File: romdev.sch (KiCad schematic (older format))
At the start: 38 parts, among them J1 AVR-ISP, J2 USB_B_Micro, J7 SYSRST, U1 ATmega328P-AU, U10 conn2k, U11 conn32k, U2 mcp2221, U3 74HCT157, U4 74HCT595, U5 74HCT595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

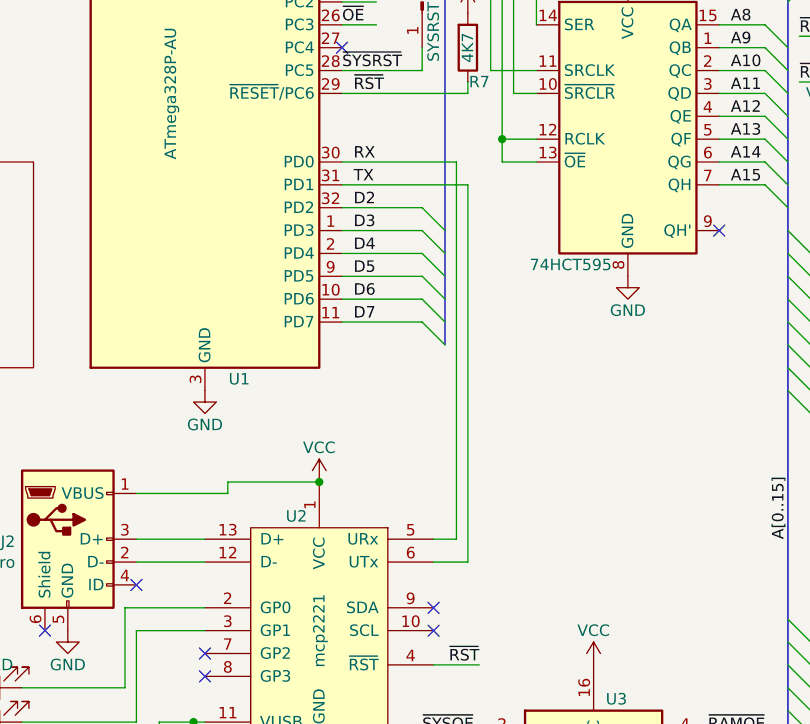
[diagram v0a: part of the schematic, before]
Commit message: fixed swapped RX/TX lines
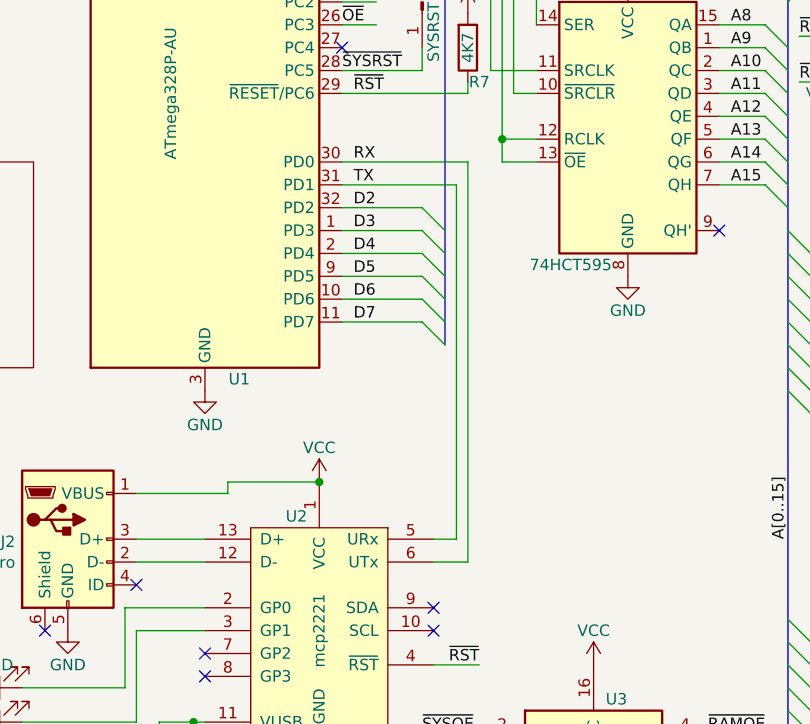
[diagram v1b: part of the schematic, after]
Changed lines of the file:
@@
 NoConn ~ 4450 3750
 Wire Wire Line
-	2800 3450 3300 3450
-Wire Wire Line
-	3300 3450 3300 5100
+	3300 3550 3300 5100
 Text Label 2850 3450 0    50   ~ 0
 RX
@@
 	3300 5100 3200 5100
 Wire Wire Line
-	3350 3550 3350 5200
-Wire Wire Line
 	3350 5200 3200 5200
-Wire Wire Line
-	2800 3550 3350 3550
 Text Label 2850 3550 0    50   ~ 0
 TX
@@
 Wire Wire Line
 	2800 3150 3350 3150
+$Comp
+L power:VCC #PWR032
+U 1 1 60FE6889
+P 3350 2800
+F 0 "#PWR032" H 3350 2650 50  0001 C CNN
+F 1 "VCC" H 3350 2950 50  0000 C CNN
+F 2 "" H 3350 2800 50  0001 C CNN
+F 3 "" H 3350 2800 50  0001 C CNN
+	1    3350 2800
+	1    0    0    -1
+$EndComp
+Wire Wire Line
+	3300 3550 2800 3550
+Wire Wire Line
+	3350 3450 2800 3450
+Wire Wire Line
+	3350 3450 3350 5200
 Wire Bus Line
 	8100 1500 8100 2650
@@
 Wire Bus Line
 	4750 1250 4750 6150
-$Comp
-L power:VCC #PWR032
-U 1 1 60FE6889
-P 3350 2800
-F 0 "#PWR032" H 3350 2650 50  0001 C CNN
-F 1 "VCC" H 3350 2950 50  0000 C CNN
-F 2 "" H 3350 2800 50  0001 C CNN
-F 3 "" H 3350 2800 50  0001 C CNN
-	1    3350 2800
-	1    0    0    -1
-$EndComp
 $EndSCHEMATC

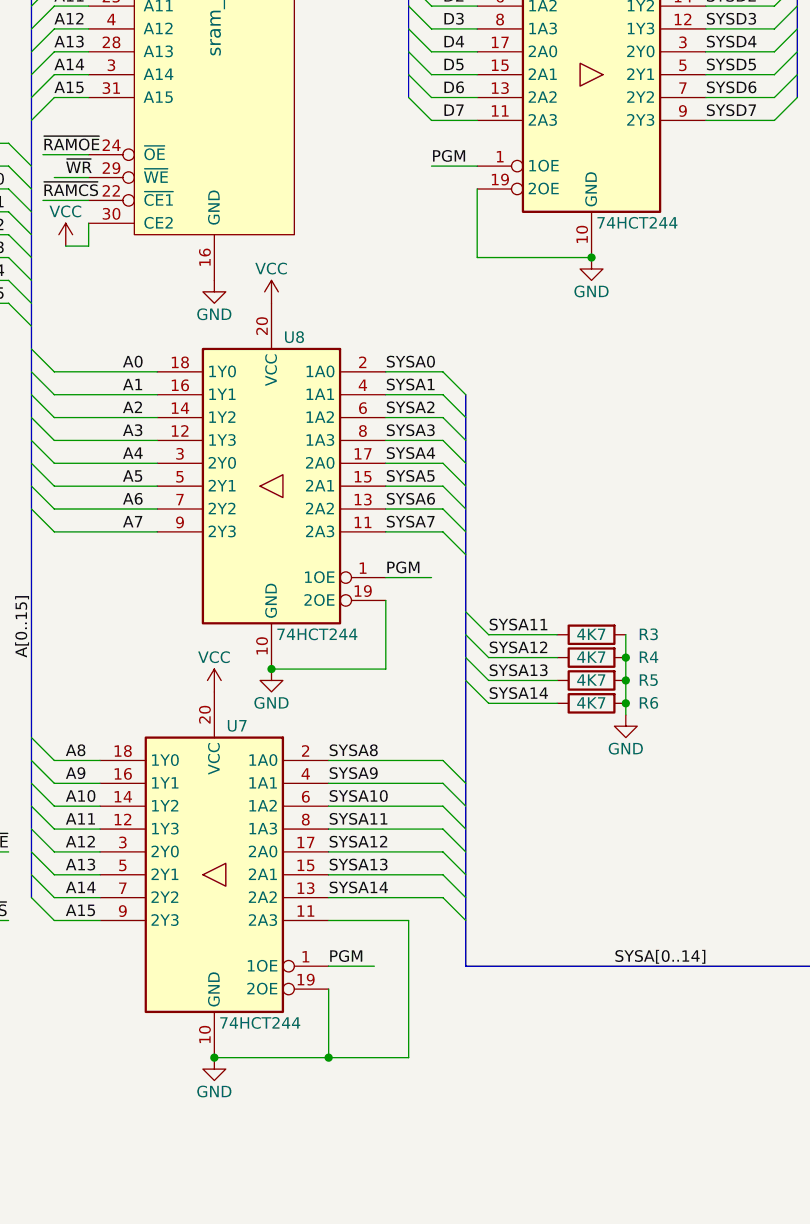
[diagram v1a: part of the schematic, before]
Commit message: - fixed mistake tying half the tri-state buffer bits to always on - fixed firmware bugs, now it can program and readback memory correctly
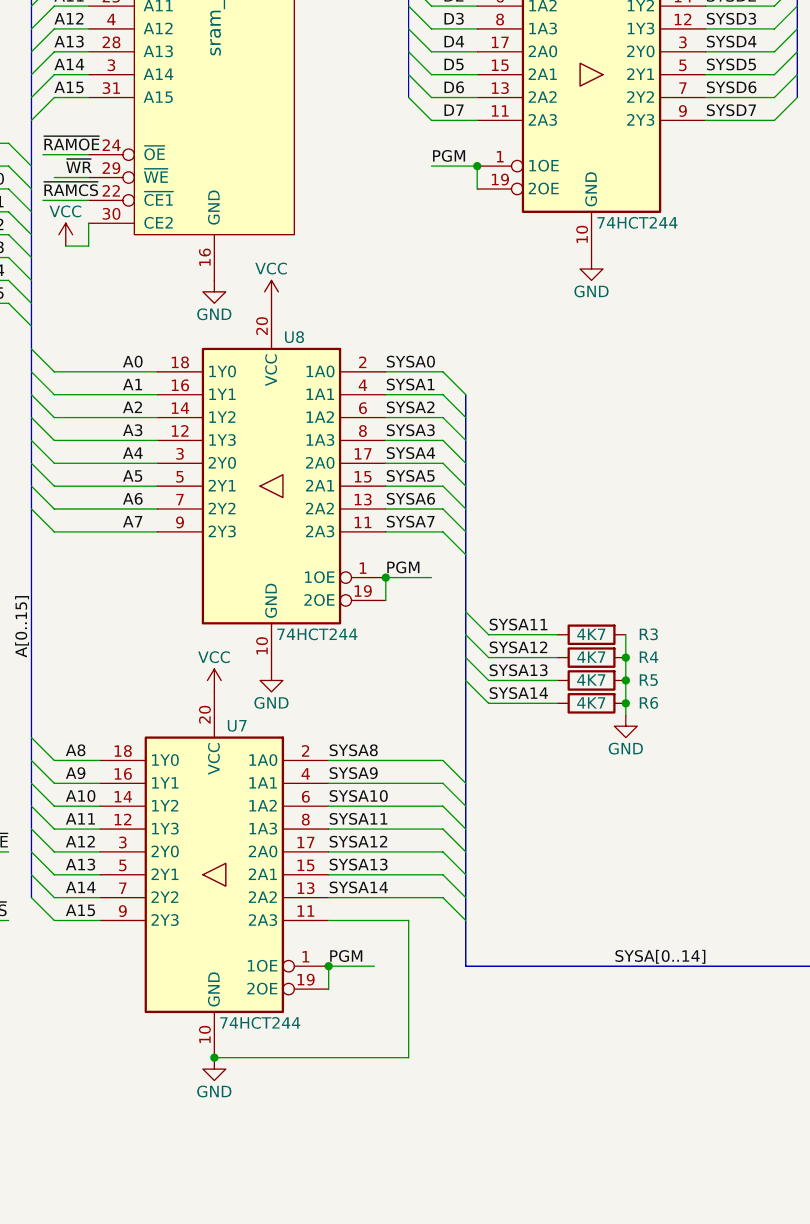
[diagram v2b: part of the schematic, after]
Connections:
- wire segments 275 -> 272
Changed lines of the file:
@@
 Wire Wire Line
 	5000 3300 5000 3200
-Wire Wire Line
-	6700 3050 6700 3350
-Wire Wire Line
-	6700 3350 7200 3350
-Connection ~ 7200 3350
-Wire Wire Line
-	6300 4850 6300 5150
-Wire Wire Line
-	6300 5150 5800 5150
-Connection ~ 5800 5150
-Wire Wire Line
-	6050 6550 6050 6850
-Wire Wire Line
-	6050 6850 5550 6850
 Connection ~ 5550 6850
 Wire Wire Line
@@
 Text Notes 7750 650  0    50   ~ 0
 bypass capacitors
-Connection ~ 6050 6850
 NoConn ~ 1900 5300
 Text Label 2800 3050 0    50   ~ 0
@@
 	6250 6450 6050 6450
 Wire Wire Line
-	6400 6850 6050 6850
-Wire Wire Line
 	6050 6250 6400 6250
 Wire Wire Line
@@
 Wire Wire Line
 	3350 3450 3350 5200
+Wire Wire Line
+	5550 6850 6400 6850
+Wire Wire Line
+	6300 4850 6300 4750
+Connection ~ 6300 4750
+Wire Wire Line
+	6050 6550 6050 6450
+Connection ~ 6050 6450
+Wire Wire Line
+	6700 3050 6700 2950
 Wire Bus Line
 	8100 1500 8100 2650
@@
 Wire Bus Line
 	4750 1250 4750 6150
+Connection ~ 6700 2950
 $EndSCHEMATC

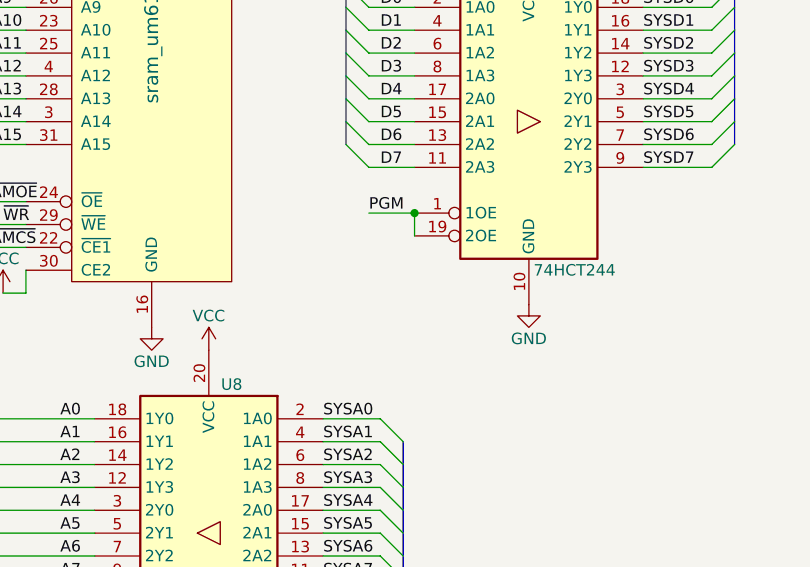
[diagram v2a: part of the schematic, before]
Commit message: fixed data bus output buffer enable
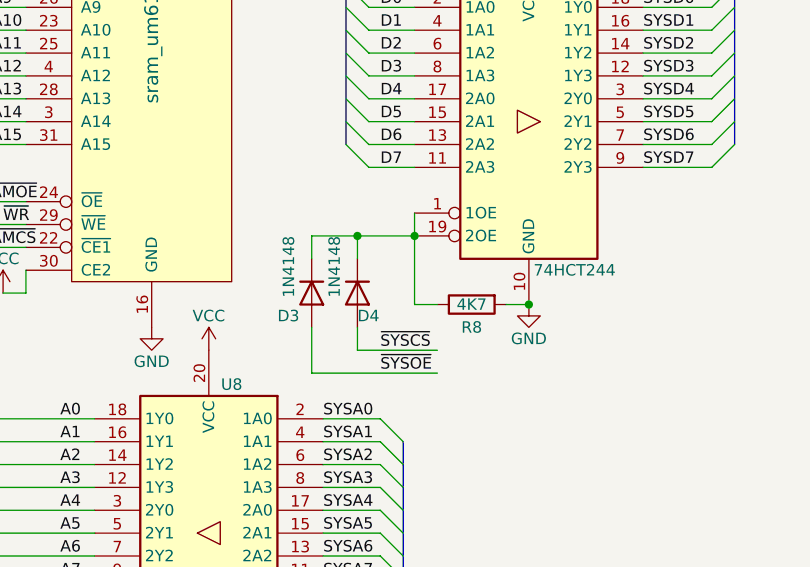
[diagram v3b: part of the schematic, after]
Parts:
- added D3, D4: 1N4148, Diode_SMD:D_0805_2012Metric_Pad1.15x1.40mm_HandSolder, symbol Diode:1N4148
- added R8: 4K7, Resistor_SMD:R_0805_2012Metric_Pad1.15x1.40mm_HandSolder, symbol Device:R
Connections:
- wire segments 272 -> 282
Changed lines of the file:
@@
-PGM
-Wire Wire Line
-	6700 2950 6500 2950
-Text Label 6500 2950 0    50   ~ 0
 PGM
 Wire Wire Line
@@
 Wire Wire Line
 	6700 3050 6700 2950
+$Comp
+L Diode:1N4148 D3
+U 1 1 5F8C7D7E
+P 6250 3300
+F 0 "D3" V 6350 3150 50  0000 L CNN
+F 1 "1N4148" H 6000 3200 50  0000 L CNN
+F 2 "Diode_SMD:D_0805_2012Metric_Pad1.15x1.40mm_HandSolder" H 6250 3125 50  0001 C CNN
+F 3 "https://assets.nexperia.com/documents/data-sheet/1N4148_1N4448.pdf" H 6250 3300 50  0001 C CNN
+	1    6250 3300
+	0    1    1    0
+$EndComp
+$Comp
+L Diode:1N4148 D4
+U 1 1 5F89552F
+P 6450 3300
+F 0 "D4" V 6550 3300 50  0000 L CNN
+F 1 "1N4148" H 6200 3200 50  0000 L CNN
+F 2 "Diode_SMD:D_0805_2012Metric_Pad1.15x1.40mm_HandSolder" H 6450 3125 50  0001 C CNN
+F 3 "https://assets.nexperia.com/documents/data-sheet/1N4148_1N4448.pdf" H 6450 3300 50  0001 C CNN
+	1    6450 3300
+	0    1    1    0
+$EndComp
+Connection ~ 6700 3050
+Text Label 6550 3550 0    50   ~ 0
+~SYSCS
+Text Label 6550 3650 0    50   ~ 0
+~SYSOE
+Wire Wire Line
+	6800 3550 6450 3550
+Wire Wire Line
+	6450 3550 6450 3450
+Wire Wire Line
+	6800 3650 6250 3650
+Wire Wire Line
+	6250 3650 6250 3450
+Wire Wire Line
+	6250 3150 6250 3050
+Wire Wire Line
+	6250 3050 6450 3050
+Wire Wire Line
+	6450 3150 6450 3050
+Connection ~ 6450 3050
+Wire Wire Line
+	6450 3050 6700 3050
+Wire Wire Line
+	6700 3350 6700 3050
+$Comp
+L Device:R R8
+U 1 1 5FB4A123
+P 6950 3350
+F 0 "R8" V 7050 3350 50  0000 C CNN
+F 1 "4K7" V 6950 3350 50  0000 C CNN
+F 2 "Resistor_SMD:R_0805_2012Metric_Pad1.15x1.40mm_HandSolder" V 6880 3350 50  0001 C CNN
+F 3 "~" H 6950 3350 50  0001 C CNN
+	1    6950 3350
+	0    -1   1    0
+$EndComp
+Wire Wire Line
+	6800 3350 6700 3350
+Wire Wire Line
+	7100 3350 7200 3350
 Wire Bus Line
 	8100 1500 8100 2650
@@
 Wire Bus Line
 	4750 1250 4750 6150
-Connection ~ 6700 2950
+Connection ~ 7200 3350
 $EndSCHEMATC
